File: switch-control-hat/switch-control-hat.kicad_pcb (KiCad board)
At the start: 2 copper layers, 85 x 56 mm, 39 parts, among them J1 Conn_01x13, J2 Conn_01x03, J3 Conn_01x02, P1 Conn_02x20_Odd_Even, U1 TLP3543, U2 TLP3543, U3 TLP3543, U4 TLP3543, U5 TLP3543, U6 TLP3543, U7 TLP3543, U8 TLP3543, U9 DS3231M

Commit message: Final board layout
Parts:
- J1: footprint Connector_Phoenix_MC:PhoenixContact_MC_1,5_13-G-3.5_1x13_P3.50mm_Horizontal -> Connector_Phoenix_MC:PhoenixContact_MC_1,5_13-G-3.81_1x13_P3.81mm_Horizontal
- J2: footprint Connector_Phoenix_MC:PhoenixContact_MC_1,5_3-G-3.5_1x03_P3.50mm_Horizontal -> Connector_Phoenix_MC:PhoenixContact_MC_1,5_3-G-3.81_1x03_P3.81mm_Horizontal
- moved J3 11.9 mm to (272.4, 130.7), turned to 90 degrees
- moved C1 4.09 mm to (265.9, 124.1)
- moved R10 4.09 mm to (267.7, 121.8)
- moved R11 4.09 mm to (267.7, 117.2)
- moved R12 4.09 mm to (267.7, 119.5)
- moved R9 4.09 mm to (267.7, 126.4)
- moved U9 4.09 mm to (276.8, 121.8)
- moved J1 1.87 mm to (209.7, 146.2)
- moved BT1 0.99 mm to (278.1, 104.8)
- moved J2 0.49 mm to (271.1, 146.2)
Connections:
- D1 pad 1: GND -> GNDA
- D2 pad 1: GND -> GNDA
- D3 pad 1: GND -> GNDA
- D4 pad 1: GND -> GNDA
- D5 pad 1: GND -> GNDA
- D6 pad 1: GND -> GNDA
- D7 pad 1: GND -> GNDA
- D8 pad 1: GND -> GNDA
- J1 pad 11: GND -> GNDA
- J1 pad 3: GND -> /ONE-WIRE
- J1 pad 5: GND -> GNDA
- J1 pad 9: /ONE-WIRE -> GNDA
- J2 pad 3: GND -> GNDA
- P1 pad 12: Net-(P1-Pad12) -> /GPIO18(GEN1)(PWM0)
- P1 pad 7: /GPIO4(GCLK) -> /ONE-WIRE
- R1 pad 2: /GPIO5 -> /GPIO18(GEN1)(PWM0)
- R2 pad 2: /GPIO12(PWM0) -> /GPIO17(GEN0)
- R3 pad 2: /GPIO6 -> /GPIO12(PWM0)
- R7 pad 2: /GPIO26 -> /GPIO20(SPI1_MOSI)
- R8 pad 2: /GPIO20(SPI1_MOSI) -> /GPIO26
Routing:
- net GNDA: track 0.00 -> 117.8 mm
- net /GPIO2(SDA1): track 6.90 -> 85.0 mm
- net +3V3: track 17.9 -> 94.0 mm
- net /GPIO3(SCL1): track 3.75 -> 76.6 mm
- net /ONE-WIRE: track 0.00 -> 48.0 mm, vias 0 -> 2
- net /GPIO5: track 40.3 -> 0.00 mm
- net /GPIO17(GEN0): track 0.00 -> 33.6 mm
- net /GPIO6: track 27.6 -> 0.00 mm
- net /GPIO12(PWM0): track 58.3 -> 31.7 mm
- net Net-(BT1-Pad1): track 9.35 -> 33.6 mm
- net /GPIO18(GEN1)(PWM0): track 0.00 -> 21.5 mm
- net /GPIO26: track 7.69 -> 23.9 mm
- net /GPIO20(SPI1_MOSI): track 25.3 -> 12.9 mm
- net Net-(J3-Pad1): track 17.7 -> 7.99 mm
- net Net-(J3-Pad2): track 19.6 -> 13.4 mm
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- added copper zone on B.Cu, net GND
- added copper zone on F.Cu, net GND

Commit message: Added gerber files and names
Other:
- board text added: "PRIZM switch control Tankiso H. Moso Nivek Ghazi"

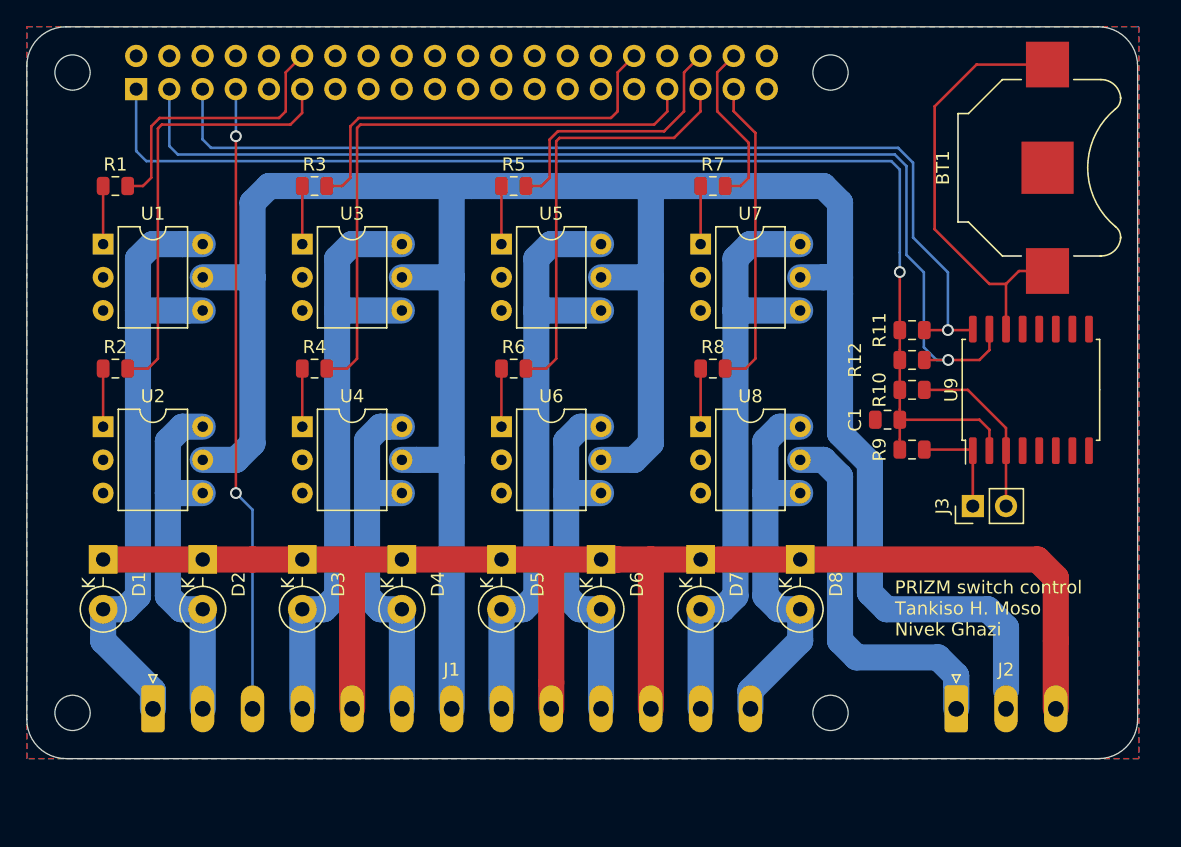
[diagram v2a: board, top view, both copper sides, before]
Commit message: fixed unrouted nets and generated gerber files for fabrication
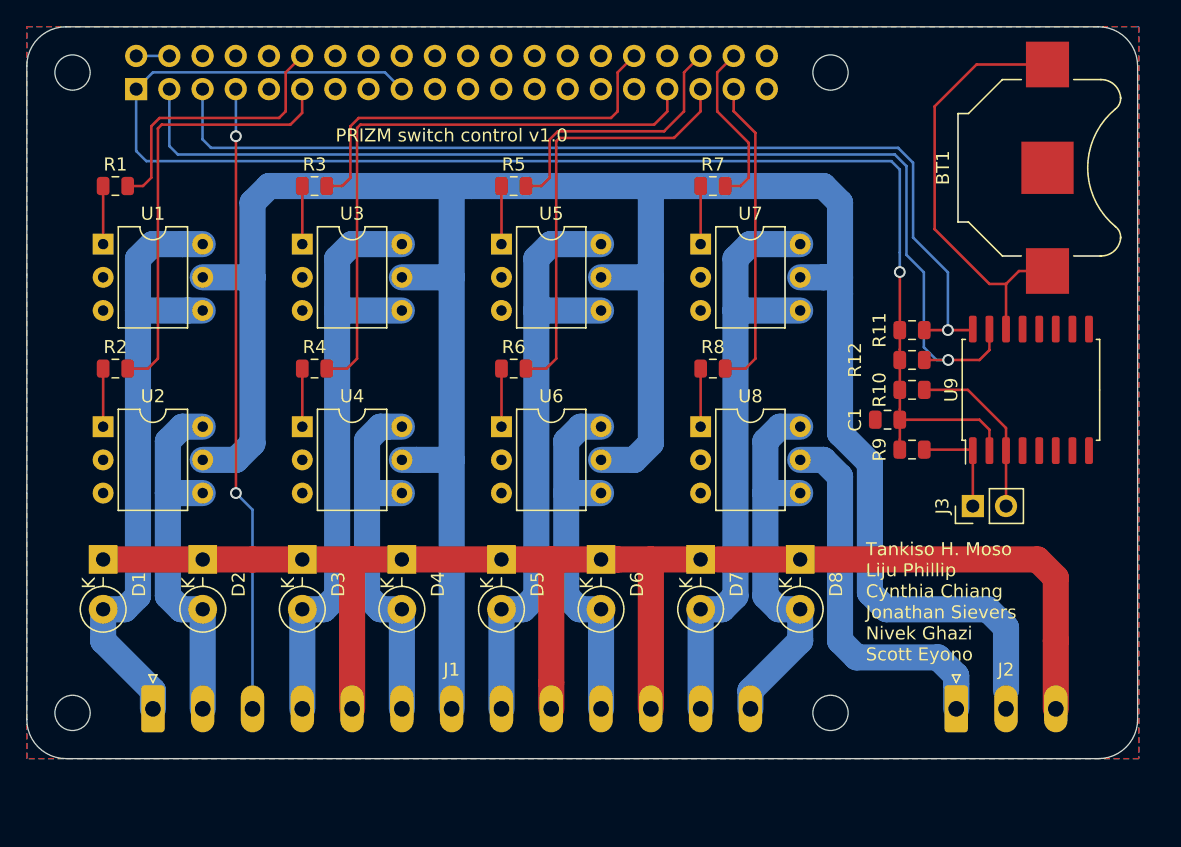
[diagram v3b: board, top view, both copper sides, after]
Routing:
- net +3V3: track 94.0 -> 115.3 mm
- net +5V: track 0.00 -> 2.54 mm
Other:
- board text added: "PRIZM switch control v1.0"
- board text added: "Tankiso H. Moso Liju Phillip Cynthia Chiang Jonathan Sievers Nivek Ghazi Scott Eyono"
- board text removed: "PRIZM switch control Tankiso H. Moso Nivek Ghazi"
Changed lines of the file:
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@@
   (general
     (thickness 1.6)
-    (drawings 11)
-    (tracks 275)
+    (drawings 12)
+    (tracks 280)
     (zones 0)
     (modules 39)
@@
     )
   )
-  (gr_text "PRIZM switch control\nTankiso H. Moso\nNivek Ghazi" (at 266.421 138.5065) (layer F.SilkS)
-    (effects (font (size 1 1) (thickness 0.25)) (justify left))
+  (gr_text "Tankiso H. Moso\nLiju Phillip\nCynthia Chiang\nJonathan Sievers\nNivek Ghazi\nScott Eyono" (at 264.1985 137.9985) (layer F.SilkS)
+    (effects (font (size 1 1) (thickness 0.15)) (justify left))
+  )
+  (gr_text "PRIZM switch control v1.0" (at 232.512 102.3115) (layer F.SilkS)
+    (effects (font (size 1 1) (thickness 0.15)))
   )
   (gr_line (start 200 97) (end 200 113) (layer Edge.Cuts) (width 0.1))
@@
   (segment (start 208.37 103.506) (end 209.144 104.28) (width 0.2) (layer B.Cu) (net 1))
   (segment (start 266.802 104.927) (end 266.802 111.265) (width 0.2) (layer B.Cu) (net 1))
+  (segment (start 227.4055 97.4855) (end 228.69 98.77) (width 0.2) (layer B.Cu) (net 1))
+  (segment (start 209.652 97.4855) (end 227.4055 97.4855) (width 0.2) (layer B.Cu) (net 1))
+  (segment (start 208.37 98.77) (end 208.37 98.7675) (width 0.2) (layer B.Cu) (net 1))
+  (segment (start 208.37 98.7675) (end 209.652 97.4855) (width 0.2) (layer B.Cu) (net 1))
+  (segment (start 210.91 96.23) (end 208.37 96.23) (width 0.2) (layer B.Cu) (net 2))
   (segment (start 254.09 100.458) (end 254.09 98.77) (width 0.2) (layer F.Cu) (net 6))
   (segment (start 255.753 102.121) (end 254.09 100.458) (width 0.2) (layer F.Cu) (net 6))

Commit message: Fixed error where optoisolators output was connected in reverse
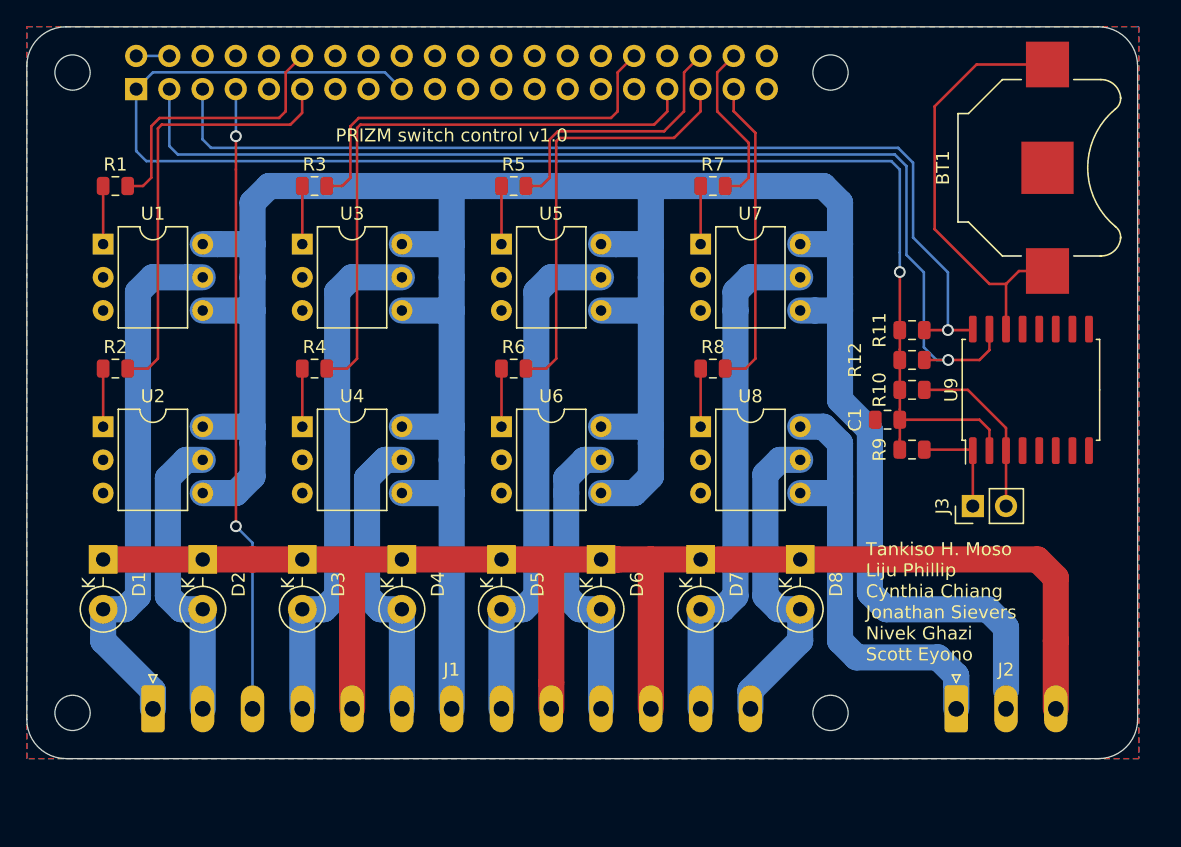
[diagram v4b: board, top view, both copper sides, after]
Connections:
- U1 pad 4: /POS1 -> +12V
- U1 pad 5: +12V -> /POS1
- U1 pad 6: /POS1 -> +12V
- U2 pad 4: /POS2 -> +12V
- U2 pad 5: +12V -> /POS2
- U2 pad 6: /POS2 -> +12V
- U3 pad 4: /POS3 -> +12V
- U3 pad 5: +12V -> /POS3
- U3 pad 6: /POS3 -> +12V
- U4 pad 4: /POS4 -> +12V
- U4 pad 5: +12V -> /POS4
- U4 pad 6: /POS4 -> +12V
- U5 pad 4: /POS5 -> +12V
- U5 pad 5: +12V -> /POS5
- U5 pad 6: /POS5 -> +12V
- U6 pad 4: /POS6 -> +12V
- U6 pad 5: +12V -> /POS6
- U6 pad 6: /POS6 -> +12V
- U7 pad 4: /RESET -> +12V
- U7 pad 5: +12V -> /RESET
- U7 pad 6: /RESET -> +12V
- U8 pad 4: /NOISE-DIODE -> +15V
- U8 pad 5: +15V -> /NOISE-DIODE
- U8 pad 6: /NOISE-DIODE -> +15V
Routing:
- net +12V: track 198.2 -> 229.2 mm
- net /RESET: track 46.9 -> 39.4 mm
- net /POS5: track 46.9 -> 39.4 mm
- net /POS3: track 46.9 -> 39.4 mm
- net /POS1: track 48.5 -> 41.0 mm
- net +15V: track 28.7 -> 34.3 mm
- net /POS2: track 28.4 -> 23.0 mm
- net /POS6: track 28.4 -> 23.0 mm
- net /NOISE-DIODE: track 29.9 -> 24.7 mm
- net /POS4: track 28.4 -> 25.0 mm

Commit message: Added pullup resistor for one-wire interface and changed 13 pin connector to 12 pin
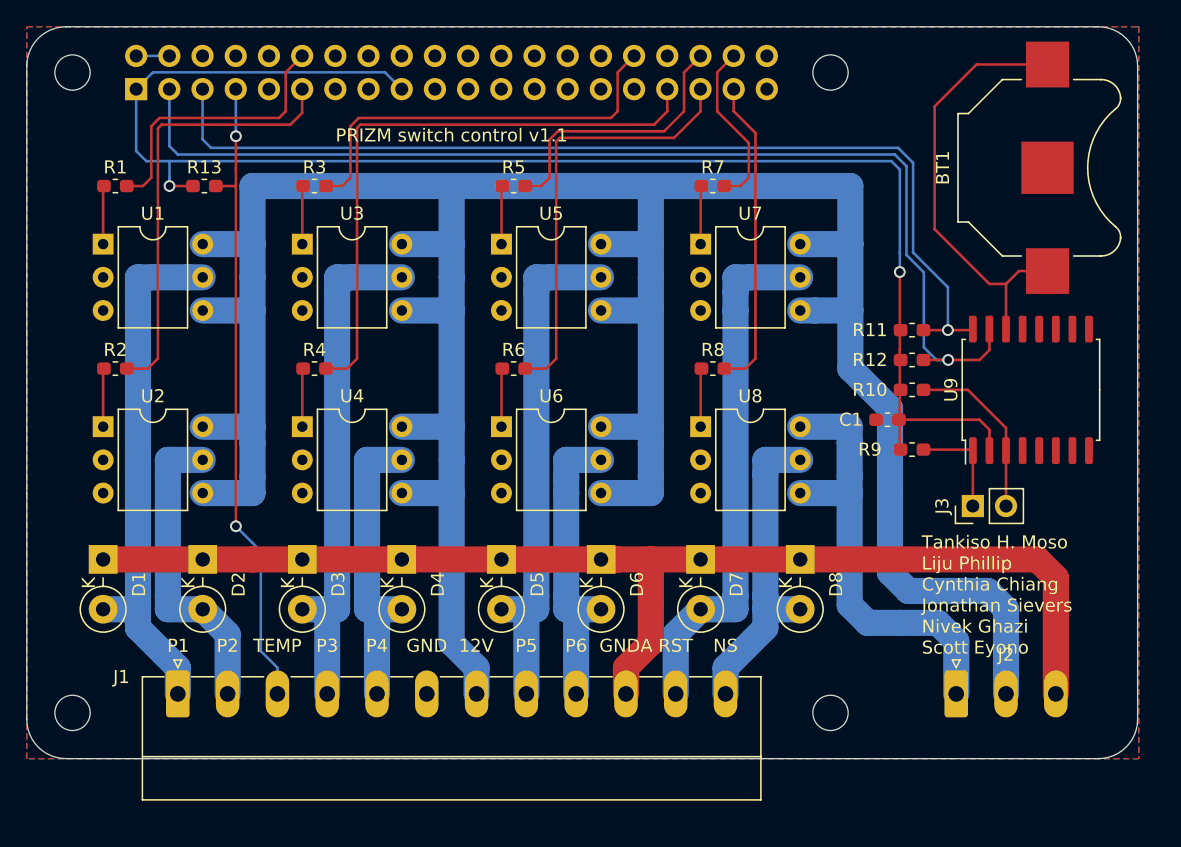
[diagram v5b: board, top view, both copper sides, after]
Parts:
- added R13: 4K7, Resistor_SMD:R_0603_1608Metric_Pad1.05x0.95mm_HandSolder, F.Cu at (213.6, 106.2)
- BT1: value Battery_Cell -> 3V
- C1: value C -> 1uF; footprint Capacitor_SMD:C_0805_2012Metric -> Capacitor_SMD:C_0603_1608Metric_Pad1.05x0.95mm_HandSolder
- D1, D2, D3, D4, D5, D6, D7, D8: value D_ALT -> 1N4001
- J1: value Conn_01x13 -> Frontend Connector; footprint Connector_Phoenix_MC:PhoenixContact_MC_1,5_13-G-3.81_1x13_P3.81mm_Horizontal -> Connector_Phoenix_MC:PhoenixContact_MC_1,5_12-G-3.81_1x12_P3.81mm_Horizontal
- J2: value Conn_01x03 -> Power Connector
- P1: value Conn_02x20_Odd_Even -> RPi-Header
- R1, R2, R3, R4, R5, R6, R7, R8: value R_US -> 200; footprint Resistor_SMD:R_0805_2012Metric -> Resistor_SMD:R_0603_1608Metric_Pad1.05x0.95mm_HandSolder
- R10, R11, R12, R9: value R_US -> 4K7; footprint Resistor_SMD:R_0805_2012Metric -> Resistor_SMD:R_0603_1608Metric_Pad1.05x0.95mm_HandSolder
- moved J1 2.22 mm to (211.6, 145.0)
- moved J2 1.14 mm to (271.1, 145.0)
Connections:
- J1 pad 10: /POS6 -> GNDA
- J1 pad 11: GNDA -> /RESET
- J1 pad 12: /RESET -> /NOISE-DIODE
- J1 pad 5: GNDA -> /POS4
- J1 pad 6: /POS4 -> GND
- J1 pad 9: GNDA -> /POS6
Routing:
- net GNDA: track 117.8 -> 93.4 mm
- net +12V: track 229.2 -> 233.1 mm
- net +3V3: track 115.3 -> 119.0 mm, vias 1 -> 2
- net /POS4: track 25.0 -> 23.3 mm
- net /ONE-WIRE: track 48.0 -> 49.1 mm
- net /POS2: track 23.0 -> 24.0 mm
- net /RESET: track 39.4 -> 40.3 mm
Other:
- board text added: "12V"
- board text added: "GND"
- board text added: "GNDA"
- board text added: "NS"
- board text added: "P1"
- board text added: "P2"
- board text added: "P3"
- board text added: "P4"
- board text added: "P5"
- board text added: "P6"
- board text added: "PRIZM switch control v1.1"
- board text added: "RST"
- board text added: "TEMP"
- board text removed: "PRIZM switch control v1.0"

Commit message: Final verision of schematic and PCB layout
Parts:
- moved C1 0.13 mm to (266.0, 124.1)
- moved R1 0.06 mm to (206.7, 106.2)
- moved R2 0.06 mm to (206.7, 120.2)
- moved R3 0.06 mm to (222.0, 106.2)
- moved R4 0.06 mm to (222.0, 120.2)
- moved R5 0.06 mm to (237.2, 106.2)
- moved R6 0.06 mm to (237.2, 120.2)
- moved R7 0.06 mm to (252.4, 106.2)
- moved R8 0.06 mm to (252.4, 120.2)
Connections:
- D1 pad 1: GNDA -> GND
- D2 pad 1: GNDA -> GND
- D3 pad 1: GNDA -> GND
- D4 pad 1: GNDA -> GND
- D5 pad 1: GNDA -> GND
- D6 pad 1: GNDA -> GND
- D7 pad 1: GNDA -> GND
- D8 pad 1: GNDA -> GND
- J1 pad 10: GNDA -> GND
- J2 pad 3: GNDA -> (no net)
- P1 pad 10: /GPIO15(RXD0) -> (no net)
- P1 pad 11: /GPIO17(GEN0) -> (no net)
- P1 pad 12: /GPIO18(GEN1)(PWM0) -> (no net)
- P1 pad 13: Net-(P1-Pad13) -> (no net)
- P1 pad 15: Net-(P1-Pad15) -> (no net)
- P1 pad 16: Net-(P1-Pad16) -> (no net)
- P1 pad 18: Net-(P1-Pad18) -> (no net)
- P1 pad 19: Net-(P1-Pad19) -> (no net)
- P1 pad 21: Net-(P1-Pad21) -> (no net)
- P1 pad 22: Net-(P1-Pad22) -> (no net)
- P1 pad 23: Net-(P1-Pad23) -> (no net)
- P1 pad 24: Net-(P1-Pad24) -> (no net)
- P1 pad 26: Net-(P1-Pad26) -> (no net)
- P1 pad 27: Net-(P1-Pad27) -> (no net)
- P1 pad 28: Net-(P1-Pad28) -> (no net)
- P1 pad 29: /GPIO5 -> (no net)
- P1 pad 8: /GPIO14(TXD0) -> (no net)
- R1 pad 2: /GPIO18(GEN1)(PWM0) -> /GPIO6
- R2 pad 2: /GPIO17(GEN0) -> /GPIO12(PWM0)
- R3 pad 2: /GPIO12(PWM0) -> /GPIO13(PWM1)
- R4 pad 2: /GPIO13(PWM1) -> /GPIO16
- R5 pad 2: /GPIO16 -> /GPIO19(SPI1_MISO)
- R6 pad 2: /GPIO19(SPI1_MISO) -> /GPIO20(SPI1_MOSI)
- R7 pad 2: /GPIO20(SPI1_MOSI) -> /GPIO26
- R8 pad 2: /GPIO26 -> /GPIO21(SPI1_SCK)
- U1 pad 3: Net-(U1-Pad3) -> (no net)
- U2 pad 3: Net-(U2-Pad3) -> (no net)
- U3 pad 3: Net-(U3-Pad3) -> (no net)
- U4 pad 3: Net-(U4-Pad3) -> (no net)
- U5 pad 3: Net-(U5-Pad3) -> (no net)
- U6 pad 3: Net-(U6-Pad3) -> (no net)
- U7 pad 3: Net-(U7-Pad3) -> (no net)
- U8 pad 3: Net-(U8-Pad3) -> (no net)
- U9 pad 4: Net-(U9-Pad4) -> (no net)
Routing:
- net GNDA: track 93.4 -> 0.00 mm
- net /GPIO6: track 0.00 -> 45.3 mm
- net /GPIO17(GEN0): track 33.6 -> 0.00 mm
- net /GPIO12(PWM0): track 31.7 -> 63.4 mm
- net /GPIO16: track 20.9 -> 49.9 mm
- net /GPIO21(SPI1_SCK): track 0.00 -> 26.9 mm
- net /GPIO20(SPI1_MOSI): track 12.9 -> 36.5 mm
- net /GPIO18(GEN1)(PWM0): track 21.5 -> 0.00 mm
- net /GPIO19(SPI1_MISO): track 33.0 -> 18.4 mm
- net /GPIO26: track 23.9 -> 9.45 mm
- net /GPIO13(PWM1): track 46.3 -> 31.8 mm
- net +12V: track 233.1 -> 234.7 mm
- net /GPIO3(SCL1): track 76.6 -> 75.0 mm
- net +3V3: track 119.0 -> 117.4 mm
- net +15V: track 34.5 -> 36.2 mm
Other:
- board text removed: "GNDA"
